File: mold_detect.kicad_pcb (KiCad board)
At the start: 2 copper layers, 37 x 68 mm, 23 parts, among them J1 ISP, SW1 watchdog_sw, U1 SHT30-DIS, U2 TPL5010, U3 ATmega328P-P

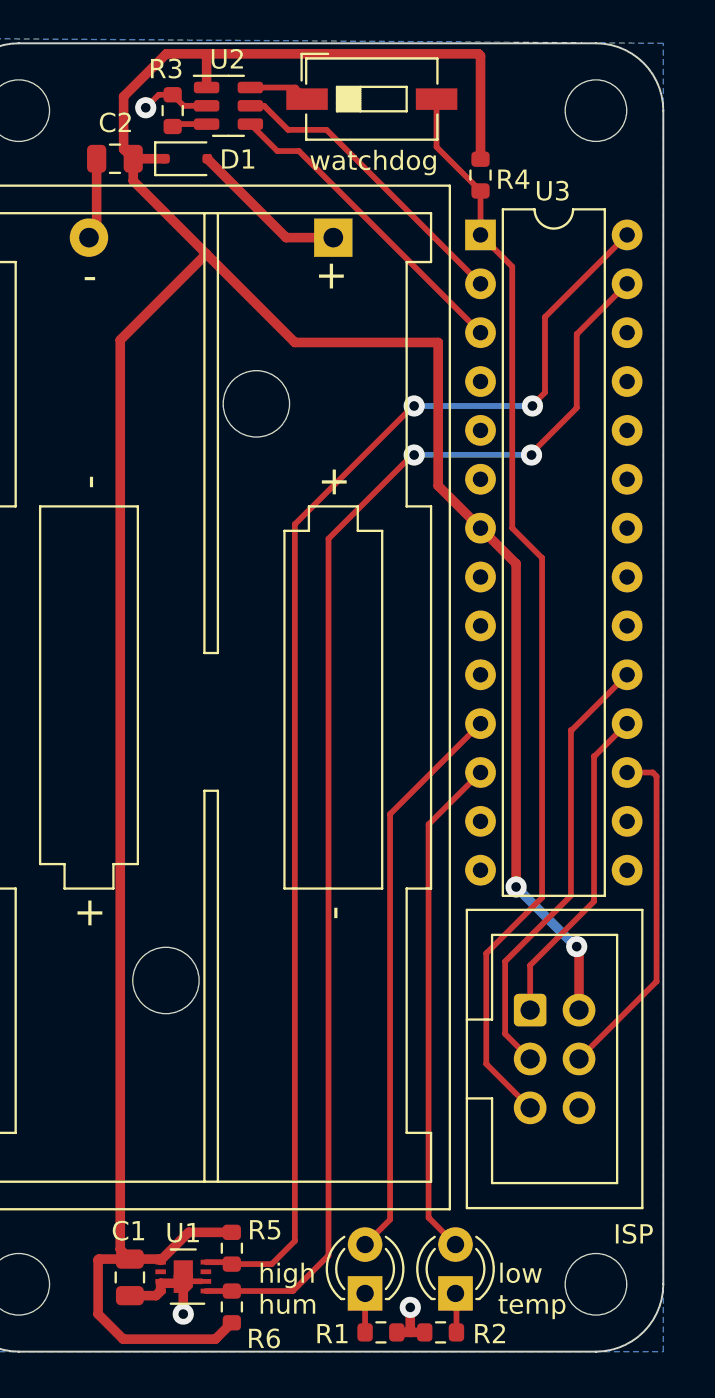
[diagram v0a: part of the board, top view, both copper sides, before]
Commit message: removed isp; added uart; added flash
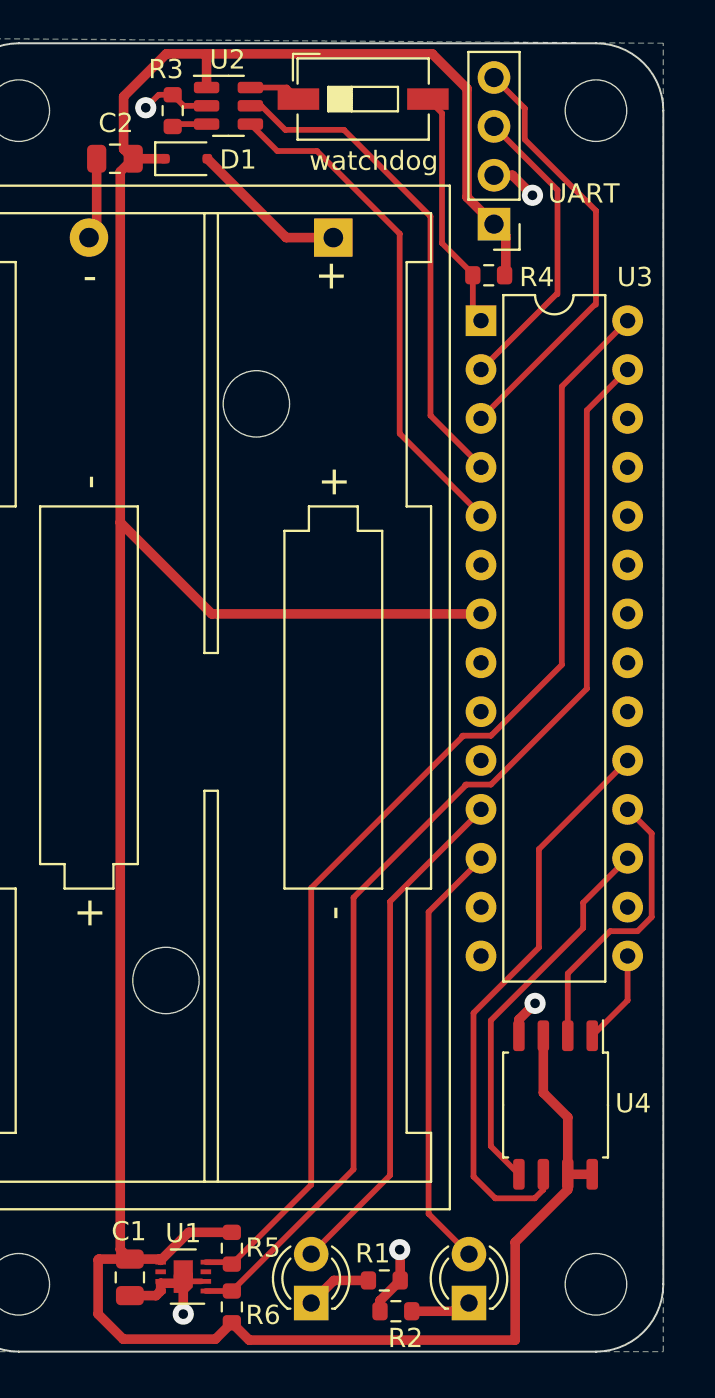
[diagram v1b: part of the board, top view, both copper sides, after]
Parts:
- removed J1: ISP, Connector_IDC:IDC-Header_2x03_P2.54mm_Vertical
- removed REF**: OSHW-Logo2_9.8x8mm_SilkScreen, Symbol:OSHW-Logo2_9.8x8mm_SilkScreen
- added J2: UART, Connector_PinHeader_2.54mm:PinHeader_1x04_P2.54mm_Vertical, F.Cu at (106.7, 88.9)
- added U4: W25Q128JVS, Package_SO:SOIC-8_5.23x5.23mm_P1.27mm, F.Cu at (109.9, 134.7)
- moved R4 5.22 mm to (106.4, 91.6), turned to 180 degrees
- moved U3 4.46 mm to (106.0, 93.9)
- moved Red1 2.84 mm to (97.2, 145.0)
- moved R1 2.71 mm to (101.0, 143.8)
- moved R2 2.57 mm to (101.6, 145.4)
- moved Blue1 0.86 mm to (105.4, 145.0)
- moved SW1 0.45 mm to (99.9, 82.4)
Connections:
- U3 pad 15: unconnected-(U3-PB1-Pad15) -> FLASH_CS
- U3 pad 2: WAKE_INTR -> RXD
- U3 pad 3: DONE -> TXD
- U3 pad 4: unconnected-(U3-PD2-Pad4) -> WAKE_INTR
- U3 pad 5: unconnected-(U3-PD3-Pad5) -> DONE
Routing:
- net RST: track 56.8 -> 12.7 mm
- net TXD: track 0.00 -> 22.4 mm
- net RXD: track 0.00 -> 15.6 mm
- net DONE: track 16.5 -> 26.6 mm
- net WAKE_INTR: track 15.8 -> 25.9 mm
- net SDA: track 67.7 -> 58.6 mm, vias 2 -> 0
- net SCL: track 68.4 -> 60.0 mm, vias 2 -> 0
- net SCK: track 23.2 -> 30.0 mm
- net GND: track 17.1 -> 22.5 mm, vias 3 -> 5
- net +3V0: track 162.6 -> 167.5 mm, vias 2 -> 0
- net FLASH_CS: track 0.00 -> 4.91 mm
- net TEMP_LED: track 26.2 -> 22.6 mm
- net HUM_LED: track 29.6 -> 26.8 mm
- net MISO: track 17.0 -> 14.9 mm
- net MOSI: track 18.0 -> 20.0 mm
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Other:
- board text added: "UART"
- board text added: "github.com/christopher-besch/mold_detect Christopher Besch <mail@chris-besch.com> designed at the Chair for Embedded Systems Rev. 1.0.0 January 2024"
- board text removed: "ISP"
- board text removed: "github.com/christopher-besch/mold_detect Christopher Besch <mail@chris-besch.com> designed at Chair for Embedded Systems Rev. 1.0.0 January 2024"
- board text removed: "high hum"
- board text removed: "low temp"

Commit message: .
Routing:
- net +3V0: track 167.5 -> 166.4 mm
- net GND: track 22.5 -> 23.5 mm
- net FLASH_CS: track 4.91 -> 5.44 mm
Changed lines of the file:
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@@
   (segment (start 105.635 138.4) (end 105.635 129.9) (width 0.3) (layer "F.Cu") (net 5))
   (segment (start 105.635 129.9) (end 109.035 126.5) (width 0.3) (layer "F.Cu") (net 5))
-  (segment (start 106.535 136.8225) (end 106.535 130.285786) (width 0.3) (layer "F.Cu") (net 6))
-  (segment (start 107.995 138.2825) (end 106.535 136.8225) (width 0.3) (layer "F.Cu") (net 6))
+  (segment (start 107.995 136.895) (end 106.535 135.435) (width 0.3) (layer "F.Cu") (net 6))
+  (segment (start 107.995 138.2825) (end 107.995 136.895) (width 0.3) (layer "F.Cu") (net 6))
+  (segment (start 106.535 130.285786) (end 111.335 125.485786) (width 0.3) (layer "F.Cu") (net 6))
   (segment (start 111.335 125.485786) (end 111.335 124.167107) (width 0.3) (layer "F.Cu") (net 6))
+  (segment (start 106.535 135.435) (end 106.535 130.285786) (width 0.3) (layer "F.Cu") (net 6))
   (segment (start 111.335 124.167107) (end 113.645 121.857107) (width 0.3) (layer "F.Cu") (net 6))
-  (segment (start 106.535 130.285786) (end 111.335 125.485786) (width 0.3) (layer "F.Cu") (net 6))
-  (segment (start 103.265 82.4) (end 104 83.135) (width 0.3) (layer "F.Cu") (net 7))
+  (segment (start 103.265 82.4) (end 103.2 82.465) (width 0.3) (layer "F.Cu") (net 7))
   (segment (start 105.6 91.557107) (end 105.6 93.492107) (width 0.3) (layer "F.Cu") (net 7))
+  (segment (start 104.3 87.2) (end 104.3 90.192107) (width 0.3) (layer "F.Cu") (net 7))
+  (segment (start 104.3 90.192107) (end 105.665 91.557107) (width 0.3) (layer "F.Cu") (net 7))
+  (segment (start 103.2 86.1) (end 104.3 87.2) (width 0.3) (layer "F.Cu") (net 7))
   (segment (start 105.6 93.492107) (end 106.025 93.917107) (width 0.3) (layer "F.Cu") (net 7))
-  (segment (start 104 89.892107) (end 105.665 91.557107) (width 0.3) (layer "F.Cu") (net 7))
-  (segment (start 104 83.135) (end 104 89.892107) (width 0.3) (layer "F.Cu") (net 7))
+  (segment (start 103.2 82.465) (end 103.2 86.1) (width 0.3) (layer "F.Cu") (net 7))
   (segment (start 87.775 142.69) (end 87.79 142.675) (width 0.5) (layer "F.Cu") (net 8))
   (segment (start 87.425 146.85) (end 86.125 145.55) (width 0.5) (layer "F.Cu") (net 8))
@@
   (segment (start 87.95 85.5) (end 87.450062 85.000062) (width 0.5) (layer "F.Cu") (net 8))
   (segment (start 91.8 80.05) (end 103.490101 80.05) (width 0.5) (layer "F.Cu") (net 8))
-  (segment (start 93.075 146) (end 93.975 146.9) (width 0.5) (layer "F.Cu") (net 8))
-  (segment (start 106.09 109.157107) (end 92.032169 109.157107) (width 0.5) (layer "F.Cu") (net 8))
   (segment (start 87.275062 86.174938) (end 87.95 85.5) (width 0.5) (layer "F.Cu") (net 8))
-  (segment (start 92.032169 109.157107) (end 87.275062 104.4) (width 0.5) (layer "F.Cu") (net 8))
   (segment (start 87.275062 142.190062) (end 87.275062 104.4) (width 0.5) (layer "F.Cu") (net 8))
   (segment (start 110.535 138.2825) (end 111.805 138.2825) (width 0.5) (layer "F.Cu") (net 8))
   (segment (start 93.075 141.3) (end 90.83 141.3) (width 0.5) (layer "F.Cu") (net 8))
-  (segment (start 107.8 141.817499) (end 110.535 139.082499) (width 0.5) (layer "F.Cu") (net 8))
-  (segment (start 110.535 139.082499) (end 110.535 138.2825) (width 0.5) (layer "F.Cu") (net 8))
+  (segment (start 107.8 145.3) (end 107.8 141.817499) (width 0.5) (layer "F.Cu") (net 8))
   (segment (start 103.490101 80.05) (end 105.3 81.859899) (width 0.5) (layer "F.Cu") (net 8))
   (segment (start 90.83 141.3) (end 89.375 142.755) (width 0.5) (layer "F.Cu") (net 8))
@@
   (segment (start 86.125 145.55) (end 86.125 142.73) (width 0.5) (layer "F.Cu") (net 8))
   (segment (start 91.7625 81.8) (end 91.7625 80.0875) (width 0.5) (layer "F.Cu") (net 8))
+  (segment (start 106.09 109.157107) (end 98.357107 109.157107) (width 0.5) (layer "F.Cu") (net 8))
+  (segment (start 93.075 146) (end 93.975 146.9) (width 0.5) (layer "F.Cu") (net 8))
   (segment (start 87.450062 82.269572) (end 89.669634 80.05) (width 0.5) (layer "F.Cu") (net 8))
   (segment (start 86.165 142.69) (end 87.775 142.69) (width 0.5) (layer "F.Cu") (net 8))
-  (segment (start 107.8 146.9) (end 107.8 141.817499) (width 0.5) (layer "F.Cu") (net 8))
-  (segment (start 93.975 146.9) (end 107.8 146.9) (width 0.5) (layer "F.Cu") (net 8))
+  (segment (start 93.6 104.4) (end 87.275062 104.4) (width 0.5) (layer "F.Cu") (net 8))
   (segment (start 107.315 91.557107) (end 107.315 89.515) (width 0.5) (layer "F.Cu") (net 8))
+  (segment (start 107.8 141.817499) (end 110.535 139.082499) (width 0.5) (layer "F.Cu") (net 8))
   (segment (start 89.669634 80.05) (end 91.8 80.05) (width 0.5) (layer "F.Cu") (net 8))
   (segment (start 105.3 87.5) (end 106.7 88.9) (width 0.5) (layer "F.Cu") (net 8))
   (segment (start 107.315 89.515) (end 106.7 88.9) (width 0.5) (layer "F.Cu") (net 8))
   (segment (start 87.775 142.69) (end 87.275062 142.190062) (width 0.5) (layer "F.Cu") (net 8))
+  (segment (start 106.3 146.8) (end 107.8 145.3) (width 0.5) (layer "F.Cu") (net 8))
+  (segment (start 110.535 139.082499) (end 110.535 138.2825) (width 0.5) (layer "F.Cu") (net 8))
+  (segment (start 98.357107 109.157107) (end 93.6 104.4) (width 0.5) (layer "F.Cu") (net 8))
   (segment (start 110.535 138.2825) (end 110.535 135.3175) (width 0.5) (layer "F.Cu") (net 8))
   (segment (start 87.275062 104.4) (end 87.275062 86.174938) (width 0.5) (layer "F.Cu") (net 8))
@@
   (segment (start 105.3 81.859899) (end 105.3 87.5) (width 0.5) (layer "F.Cu") (net 8))
   (segment (start 109.265 134.0475) (end 109.265 131.0825) (width 0.5) (layer "F.Cu") (net 8))
+  (segment (start 93.975 146.9) (end 106.2 146.9) (width 0.5) (layer "F.Cu") (net 8))
   (segment (start 101.3 124.107107) (end 106.09 119.317107) (width 0.3) (layer "F.Cu") (net 9))
   (segment (start 101.3 138.335) (end 97.2 142.435) (width 0.3) (layer "F.Cu") (net 9))
@@
   (segment (start 95.9 89.6) (end 98.35 89.6) (width 0.5) (layer "F.Cu") (net 10))
   (segment (start 91.8 85.5) (end 95.9 89.6) (width 0.5) (layer "F.Cu") (net 10))
-  (segment (start 94.0375 83.7) (end 95.4375 85.1) (width 0.3) (layer "F.Cu") (net 11))
+  (segment (start 101.8 99.787107) (end 106.09 104.077107) (width 0.3) (layer "F.Cu") (net 11))
+  (segment (start 97.5 85.1) (end 101.8 89.4) (width 0.3) (layer "F.Cu") (net 11))
+  (segment (start 95.8 85.1) (end 97.5 85.1) (width 0.3) (layer "F.Cu") (net 11))
   (segment (start 101.8 89.4) (end 101.8 99.787107) (width 0.3) (layer "F.Cu") (net 11))
-  (segment (start 97.5 85.1) (end 101.8 89.4) (width 0.3) (layer "F.Cu") (net 11))
-  (segment (start 101.8 99.787107) (end 106.09 104.077107) (width 0.3) (layer "F.Cu") (net 11))
-  (segment (start 95.4375 85.1) (end 97.5 85.1) (width 0.3) (layer "F.Cu") (net 11))
+  (segment (start 94.4 83.7) (end 95.8 85.1) (width 0.3) (layer "F.Cu") (net 11))
+  (segment (start 94.0375 83.7) (end 94.4 83.7) (width 0.3) (layer "F.Cu") (net 11))
   (segment (start 103.4 88.5) (end 98.9 84) (width 0.3) (layer "F.Cu") (net 12))
   (segment (start 95.852684 84) (end 94.602684 82.75) (width 0.3) (layer "F.Cu") (net 12))
@@
   (segment (start 86.05 89.2) (end 85.65 89.6) (width 0.5) (layer "F.Cu") (net 13))
   (segment (start 106.7 86.36) (end 107.66 86.36) (width 0.5) (layer "F.Cu") (net 13))
-  (segment (start 90.55 145.55) (end 90.55 143.6) (width 0.5) (layer "F.Cu") (net 13))
   (segment (start 87.775 144.59) (end 89.135 144.59) (width 0.5) (layer "F.Cu") (net 13))
   (segment (start 89.275 82.175) (end 90 82.175) (width 0.3) (layer "F.Cu") (net 13))
   (segment (start 90.205 143.945) (end 89.375 143.945) (width 0.5) (layer "F.Cu") (net 13))
+  (segment (start 89.6 145.75) (end 87.775 145.75) (width 0.5) (layer "F.Cu") (net 13))
   (segment (start 89.375 144.35) (end 89.375 143.945) (width 0.5) (layer "F.Cu") (net 13))
   (segment (start 101.825 143.8) (end 101.825 142.225) (width 0.5) (layer "F.Cu") (net 13))
@@
   (segment (start 90.575 82.75) (end 90 82.175) (width 0.3) (layer "F.Cu") (net 13))
   (segment (start 107.995 131.0825) (end 107.995 130.24) (width 0.5) (layer "F.Cu") (net 13))
+  (segment (start 87.775 145.75) (end 87.775 144.59) (width 0.5) (layer "F.Cu") (net 13))
   (segment (start 89.135 144.59) (end 89.375 144.35) (width 0.5) (layer "F.Cu") (net 13))
   (segment (start 86.05 85.5) (end 86.05 89.2) (width 0.5) (layer "F.Cu") (net 13))
@@
   (via (at 88.6 82.85) (size 1.1) (drill 0.5) (layers "F.Cu" "B.Cu") (net 13))
   (via (at 108.835 129.4) (size 1.1) (drill 0.5) (layers "F.Cu" "B.Cu") (net 13))
-  (via (at 90.55 145.55) (size 1.1) (drill 0.5) (layers "F.Cu" "B.Cu") (net 13))
+  (via (at 89.6 145.75) (size 1.1) (drill 0.5) (layers "F.Cu" "B.Cu") (net 13))
   (via (at 101.8 142.2) (size 1.1) (drill 0.5) (layers "F.Cu" "B.Cu") (net 13))
   (via (at 108.7 87.4) (size 1.1) (drill 0.5) (layers "F.Cu" "B.Cu") (net 13))
@@
   (segment (start 108.3 82.88) (end 108.3 84.5) (width 0.3) (layer "F.Cu") (net 31))
   (segment (start 106.065 98.957107) (end 106.025 98.997107) (width 0.3) (layer "B.Cu") (net 31))
-  (segment (start 113.645 126.937107) (end 113.645 129.2425) (width 0.3) (layer "F.Cu") (net 33))
-  (segment (start 113.645 129.2425) (end 111.805 131.0825) (width 0.3) (layer "F.Cu") (net 33))
+  (segment (start 113.645 130.155) (end 112.7175 131.0825) (width 0.3) (layer "F.Cu") (net 33))
+  (segment (start 112.7175 131.0825) (end 111.805 131.0825) (width 0.3) (layer "F.Cu") (net 33))
+  (segment (start 113.645 126.937107) (end 113.645 130.155) (width 0.3) (layer "F.Cu") (net 33))
   (segment (start 95.935 81.8) (end 96.535 82.4) (width 0.3) (layer "F.Cu") (net 34))
   (segment (start 94.0375 81.8) (end 95.935 81.8) (width 0.3) (layer "F.Cu") (net 34))

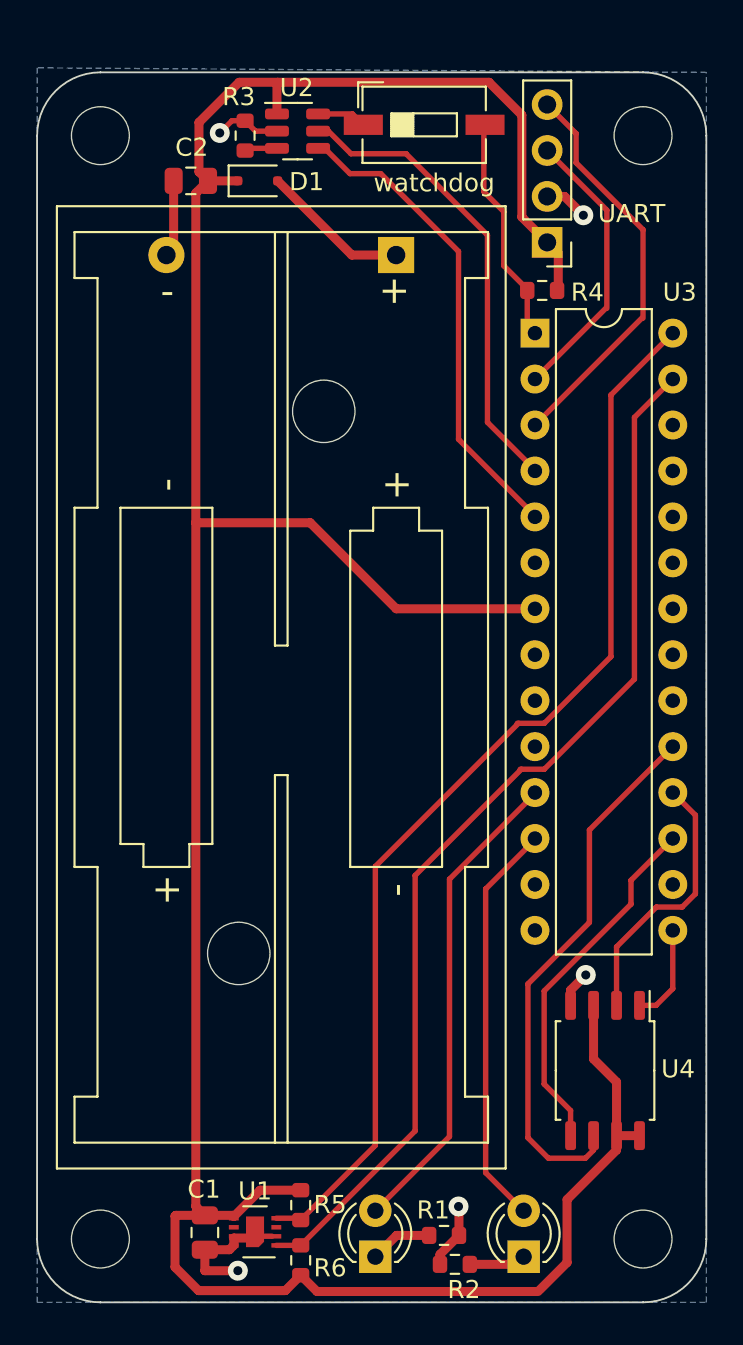
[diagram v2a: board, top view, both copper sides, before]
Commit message: added usb c port
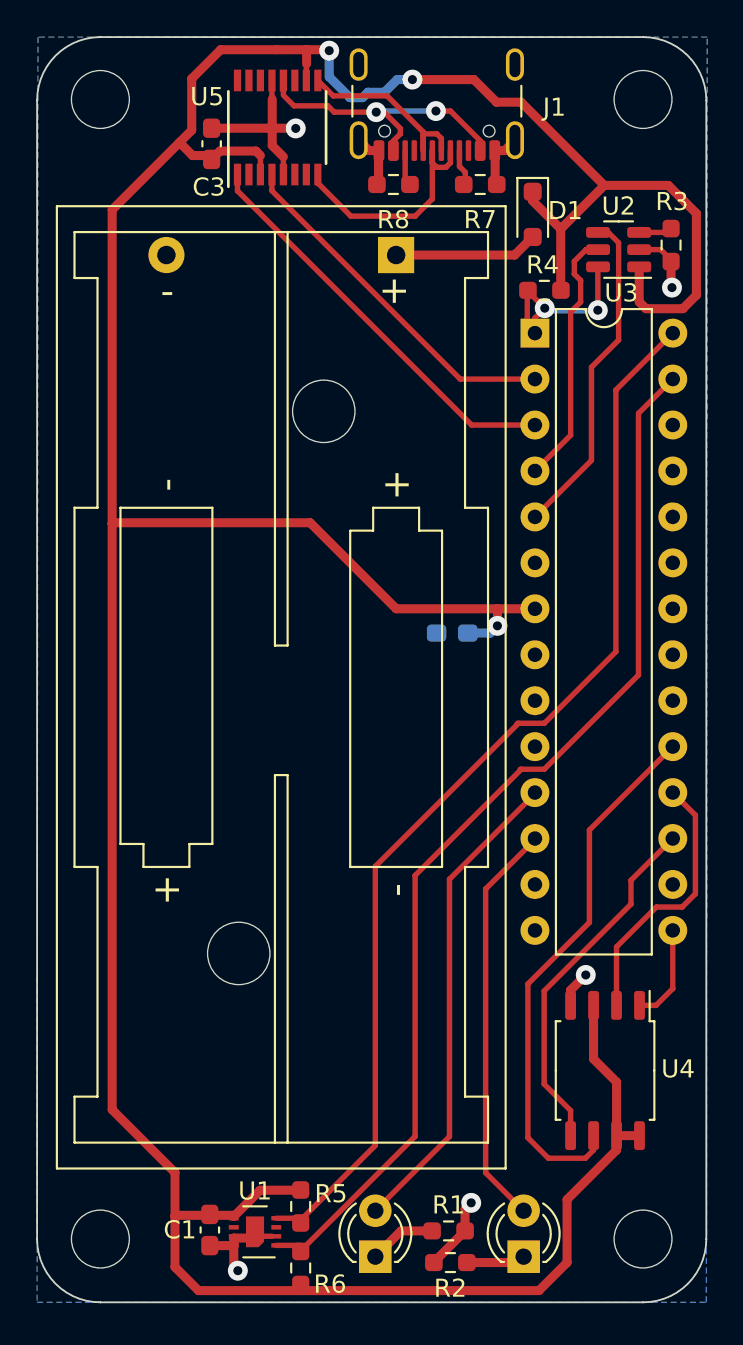
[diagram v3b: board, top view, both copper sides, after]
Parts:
- removed J2: UART, Connector_PinHeader_2.54mm:PinHeader_1x04_P2.54mm_Vertical
- removed SW1: watchdog_sw, Button_Switch_SMD:SW_DIP_SPSTx01_Slide_6.7x4.1mm_W6.73mm_P2.54mm_LowProfile_JPin
- added C3: 100n, Capacitor_SMD:C_0603_1608Metric_Pad1.08x0.95mm_HandSolder, F.Cu at (88.2, 83.5)
- added J1: USB_C_Receptacle_USB2.0_14P, Connector_USB:USB_C_Receptacle_GCT_USB4105-xx-A_16P_TopMnt_Horizontal, F.Cu at (100.6, 80.1)
- added R7: 5k1, Resistor_SMD:R_0603_1608Metric_Pad0.98x0.95mm_HandSolder, F.Cu at (103.0, 85.7)
- added R8: 5k1, Resistor_SMD:R_0603_1608Metric_Pad0.98x0.95mm_HandSolder, F.Cu at (98.2, 85.7)
- added U5: FT230XS, Package_SO:SSOP-16_3.9x4.9mm_P0.635mm, F.Cu at (91.8, 82.5)
- C1: footprint Capacitor_SMD:C_0805_2012Metric -> Capacitor_SMD:C_0603_1608Metric_Pad1.08x0.95mm_HandSolder
- C2: value 10u -> 100n; footprint Capacitor_SMD:C_0805_2012Metric -> Capacitor_SMD:C_0603_1608Metric_Pad1.08x0.95mm_HandSolder; moved to B.Cu
- D1: footprint Diode_SMD:D_SOD-323F -> Diode_SMD:D_SOD-323_HandSoldering
- R1, R2, R3, R4, R5, R6: footprint Resistor_SMD:R_0603_1608Metric -> Resistor_SMD:R_0603_1608Metric_Pad0.98x0.95mm_HandSolder
- moved C2 28.9 mm to (101.5, 110.5), turned to 0 degrees
- moved R3 24.3 mm to (113.5, 89.0), turned to -90 degrees
- moved U2 18.9 mm to (110.7, 89.3), turned to 180 degrees
- moved D1 15.3 mm to (105.9, 87.3), turned to -90 degrees
- moved H2 2.00 mm to (82.0, 81.0)
- moved H4 2.00 mm to (112.0, 81.0)
- moved R6 0.42 mm to (93.1, 145.6)
- moved R1 0.35 mm to (101.2, 143.6)
- moved C1 0.31 mm to (88.0, 143.5)
- moved R2 0.27 mm to (101.3, 145.3)
- moved R4 0.13 mm to (106.5, 91.5)
- moved R5 0.07 mm to (93.1, 142.2)
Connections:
- C2 pad 1: +3V0 -> GND
- C2 pad 2: GND -> +3V0
- U2 pad 6: Net-(SW1-A) -> RST
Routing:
- net +3V0: track 166.4 -> 206.1 mm, vias 0 -> 3
- net Net-(U5-VCC): track 0.00 -> 16.3 mm, vias 0 -> 2
- net Net-(U5-USBDP): track 0.00 -> 13.2 mm
- net WAKE_INTR: track 25.9 -> 14.4 mm
- net Net-(U5-USBDM): track 0.00 -> 10.7 mm
- net GND: track 23.5 -> 32.7 mm
- net DONE: track 26.6 -> 18.8 mm
- net RXD: track 15.6 -> 19.8 mm
- net Net-(SW1-A): track 2.75 -> 0.00 mm
- net Net-(J1-CC1): track 0.00 -> 2.05 mm
- net Net-(J1-CC2): track 0.00 -> 1.89 mm
- net RST: track 12.7 -> 10.9 mm, vias 0 -> 2
- net Net-(Blue1-K): track 3.15 -> 3.87 mm
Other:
- board size 37 x 68 mm -> 37 x 70 mm
- board text removed: "UART"
- board text removed: "watchdog"
